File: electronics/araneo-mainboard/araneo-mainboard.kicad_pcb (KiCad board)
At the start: 2 copper layers, 71.5 x 68.5 mm, 77 parts, among them J1 GPIO2, J2 OLED, J3 GPIO1, SW2 SW, SW3 SW, U1 IMU, U3 TLV1117-ADJ, U4 POWER, U5 PAM8403D

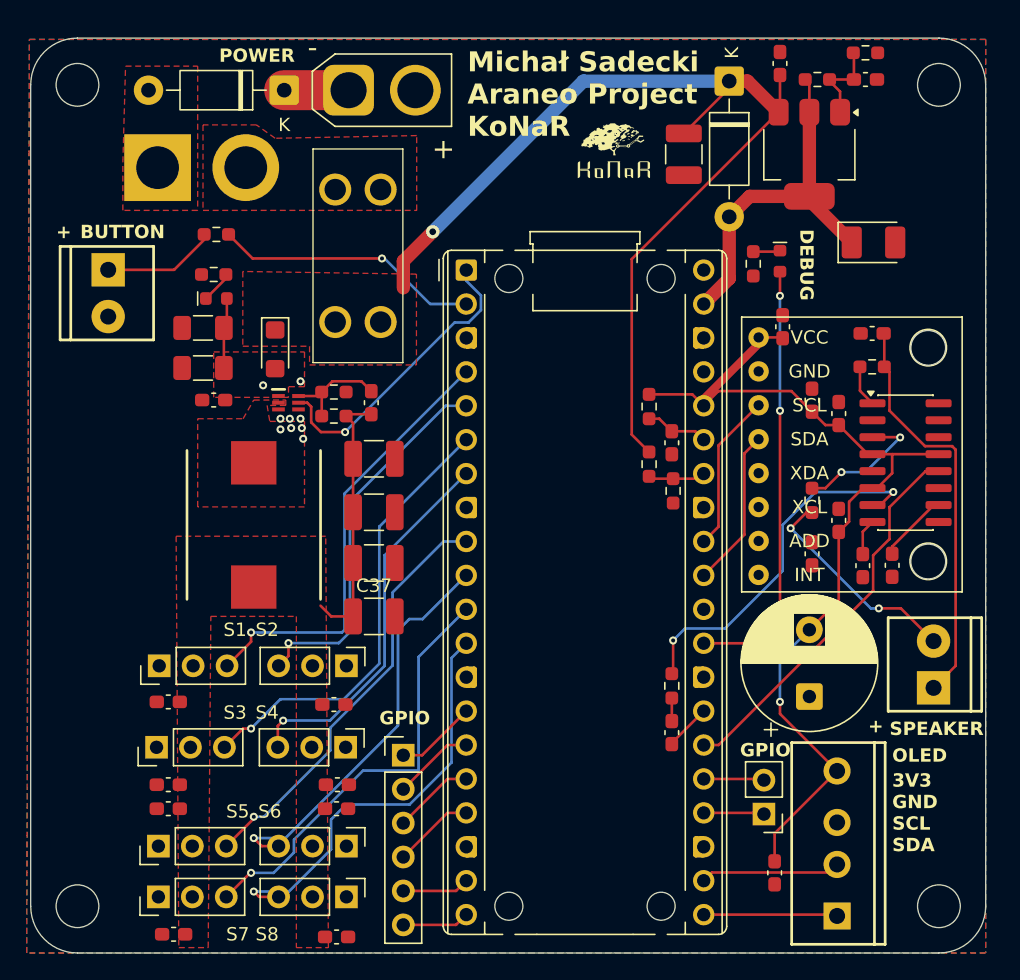
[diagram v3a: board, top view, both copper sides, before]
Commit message: electronics: add bmi270 and second buck
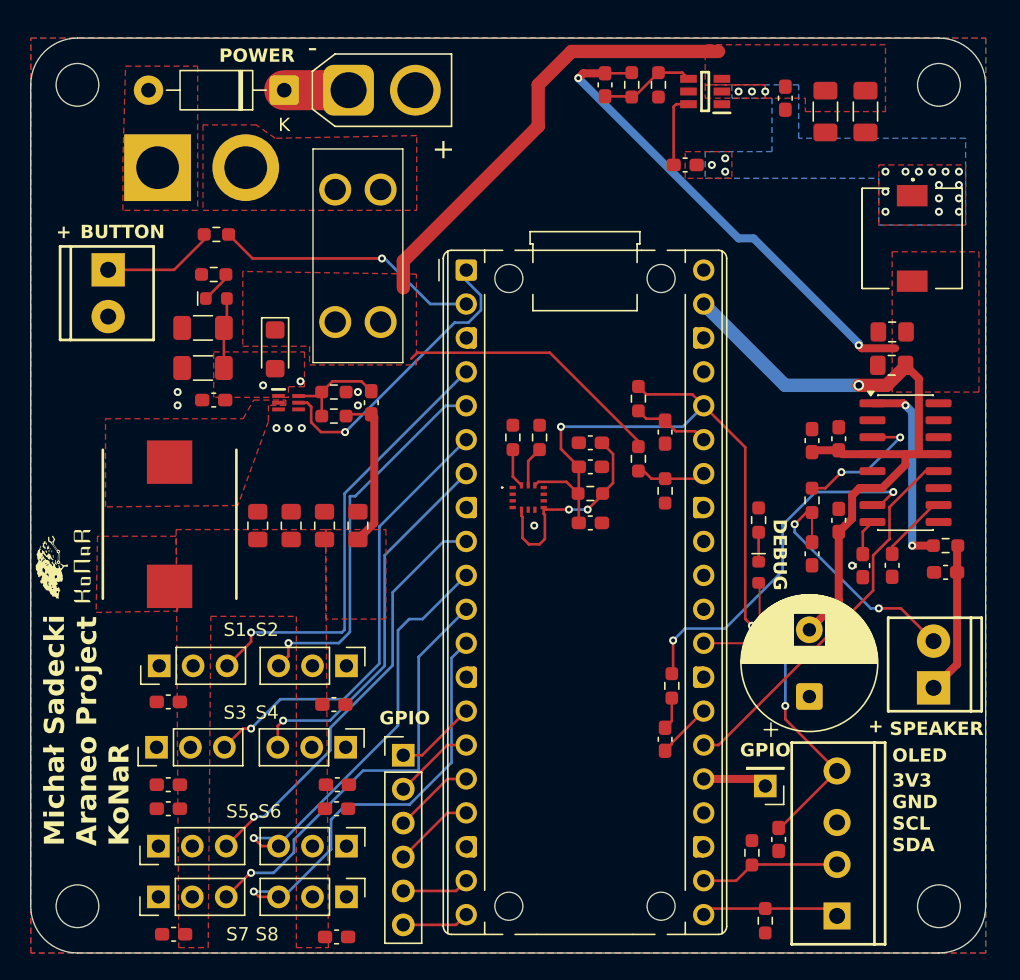
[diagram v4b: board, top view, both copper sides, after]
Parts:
- removed C2: 22uF, Capacitor_SMD:C_1210_3225Metric_Pad1.33x2.70mm_HandSolder
- removed D1: D, Diode_THT:D_DO-41_SOD81_P10.16mm_Horizontal
- removed R4: 120, Resistor_SMD:R_0603_1608Metric_Pad0.98x0.95mm_HandSolder
- removed R5: 360, Resistor_SMD:R_0603_1608Metric_Pad0.98x0.95mm_HandSolder
- removed U1: IMU, usini_sensors:module_mpu6050
- removed U3: TLV1117-ADJ, Package_TO_SOT_SMD:SOT-223-3_TabPin2
- added C35: 0.1u, Capacitor_SMD:C_0603_1608Metric_Pad1.08x0.95mm_HandSolder, F.Cu at (148.0, 40.0)
- added C39: 10u, Capacitor_SMD:C_1206_3216Metric_Pad1.33x1.80mm_HandSolder, F.Cu at (151.0, 41.0)
- added C40: 10u, Capacitor_SMD:C_1206_3216Metric_Pad1.33x1.80mm_HandSolder, F.Cu at (154.0, 41.0)
- added C41: 100p, Capacitor_SMD:C_0603_1608Metric_Pad1.08x0.95mm_HandSolder, F.Cu at (134.5, 39.0)
- added C42: 0.1u, Capacitor_SMD:C_0603_1608Metric_Pad1.08x0.95mm_HandSolder, F.Cu at (133.4, 67.6)
- added C43: 1u, Capacitor_SMD:C_0603_1608Metric_Pad1.08x0.95mm_HandSolder, F.Cu at (133.4, 71.8)
- added FB4: FerriteBead, Resistor_SMD:R_0603_1608Metric_Pad0.98x0.95mm_HandSolder, F.Cu at (133.4, 69.6)
- added IC1: TPS54302DDCR, custom_footprints:SOT95P280X110-6N, F.Cu at (142.0, 39.5)
- added IC2: BMI270, custom_footprints:BMI270, F.Cu at (128.8, 69.9)
- added L2: 10u, custom_footprints:PA4302103NLT, F.Cu at (157.5, 50.5)
- added R1: 4.7k, Resistor_SMD:R_0603_1608Metric_Pad0.98x0.95mm_HandSolder, F.Cu at (129.6, 65.4)
- added R16: 100k, Resistor_SMD:R_0603_1608Metric_Pad0.98x0.95mm_HandSolder, F.Cu at (136.5, 39.0)
- added R17: 13.3k, Resistor_SMD:R_0603_1608Metric_Pad0.98x0.95mm_HandSolder, F.Cu at (138.5, 39.0)
- added R18: 4.7k, Resistor_SMD:R_0603_1608Metric_Pad0.98x0.95mm_HandSolder, F.Cu at (146.5, 101.6)
- added R19: 4.7k, Resistor_SMD:R_0603_1608Metric_Pad0.98x0.95mm_HandSolder, F.Cu at (145.5, 96.5)
- added R2: 4.7k, Resistor_SMD:R_0603_1608Metric_Pad0.98x0.95mm_HandSolder, F.Cu at (127.6, 65.4)
- C1: value 22uF -> 0.1u; footprint Capacitor_Tantalum_SMD:CP_EIA-3528-15_AVX-H_HandSolder -> Capacitor_SMD:C_0603_1608Metric_Pad1.08x0.95mm_HandSolder
- C20: value 0.1uF -> 0.1u
- C29: value 1uF -> 22u; footprint Capacitor_SMD:C_0603_1608Metric_Pad1.08x0.95mm_HandSolder -> Capacitor_SMD:C_0805_2012Metric_Pad1.18x1.45mm_HandSolder
- C30: value 100nF -> 22u; footprint Capacitor_SMD:C_0603_1608Metric_Pad1.08x0.95mm_HandSolder -> Capacitor_SMD:C_0805_2012Metric_Pad1.18x1.45mm_HandSolder
- C34, C36, C37, C38: footprint Capacitor_SMD:C_1210_3225Metric_Pad1.33x2.70mm_HandSolder -> Capacitor_SMD:C_0805_2012Metric_Pad1.18x1.45mm_HandSolder
- C9: value 100nF -> 0.1u
- J3: footprint Connector_PinHeader_2.54mm:PinHeader_1x02_P2.54mm_Vertical -> Connector_PinHeader_2.54mm:PinHeader_1x01_P2.54mm_Vertical
- moved konar1 51.6 mm to (94.0, 75.0), turned to 90 degrees
- moved C1 26.0 mm to (133.4, 65.8)
- moved C30 24.1 mm to (156.0, 60.0), turned to 180 degrees
- moved D3 23.4 mm to (146.0, 75.5)
- moved R13 19.2 mm to (146.0, 71.6), turned to 90 degrees
- moved C29 19.0 mm to (156.0, 57.5), turned to 180 degrees
- moved C11 18.7 mm to (160.0, 75.5)
- moved FB1 14.5 mm to (160.0, 73.5)
- moved C20 14.1 mm to (140.5, 45.0), turned to 180 degrees
- moved C37 11.0 mm to (108.5, 72.0), turned to 90 degrees
- moved C36 6.80 mm to (111.0, 72.0), turned to 90 degrees
- moved L1 6.30 mm to (101.9, 71.9)
- moved C34 5.14 mm to (116.0, 72.0), turned to 90 degrees
- moved C38 3.83 mm to (113.5, 72.0), turned to 90 degrees
- moved C18 3.03 mm to (150.0, 65.6)
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- gave numbers to parts that had none: 1
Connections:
- A1 pad 24: /GPIO18 -> /IMU_INT1
- A1 pad 31: /SDA_IMU -> /IMU_SDA
- A1 pad 32: /SCL_IMU -> /IMU_SCL
- C1 pad 1: +5V -> GND
- C1 pad 2: GND -> Net-(IC2-VDD)
- C15 pad 1: +3V3 -> +5V
- C16 pad 2: +3V3 -> +5V
- C17 pad 2: +3V3 -> +5V
- C18 pad 2: +3V3 -> +5V
- C20 pad 1: +3V3 -> Net-(IC1-SW)
- C20 pad 2: GND -> Net-(IC1-BOOT)
- C29 pad 1: Net-(U3-ADJ) -> +5V
- C30 pad 1: +7.4V_F -> +5V
- J3 pad 1: /GPIO18 -> /GPIO19
- U5 pad 13: +3V3 -> +5V
- U5 pad 4: +3V3 -> +5V
- U5 pad 6: +3V3 -> +5V
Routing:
- net +5V: track 27.6 -> 88.5 mm, vias 0 -> 3
- net /D1: track 32.9 -> 8.11 mm, vias 2 -> 0
- net +7.4V_F: track 75.3 -> 54.3 mm, vias 1 -> 0
- net Net-(C11-Pad2): track 30.6 -> 11.4 mm
- net Net-(IC2-VDD): track 0.00 -> 16.1 mm, vias 0 -> 2
- net /SDA_IMU: track 11.9 -> 0.00 mm
- net /SCL_IMU: track 11.9 -> 0.00 mm
- net Net-(U5-LOUT+): track 3.12 -> 14.8 mm, vias 0 -> 2
- net +6V: track 19.9 -> 11.9 mm
- net Net-(IC1-FB): track 0.00 -> 7.22 mm
- net Net-(U3-ADJ): track 6.62 -> 0.00 mm
- net +3V3: track 71.5 -> 66.0 mm, vias 1 -> 3
- net Net-(IC1-BOOT): track 0.00 -> 5.55 mm
- net /GPIO18: track 4.55 -> 0.00 mm
- net /IMU/IMU_SCL: track 0.00 -> 3.03 mm
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- added copper zone on F.Cu, net +5V
- added copper zone on B.Cu, net Net-(IC1-SW)
- added copper zone on F.Cu, net Net-(IC1-SW)
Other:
- board text added: "15.07.2026-04.08.2026 Projekt inżynierski prowadzony przez Mateusza Cholewińskiego"
- board text removed: "22.07.2026 Projekt inżynierski prowadzony przez Mateusza Cholewińskiego"

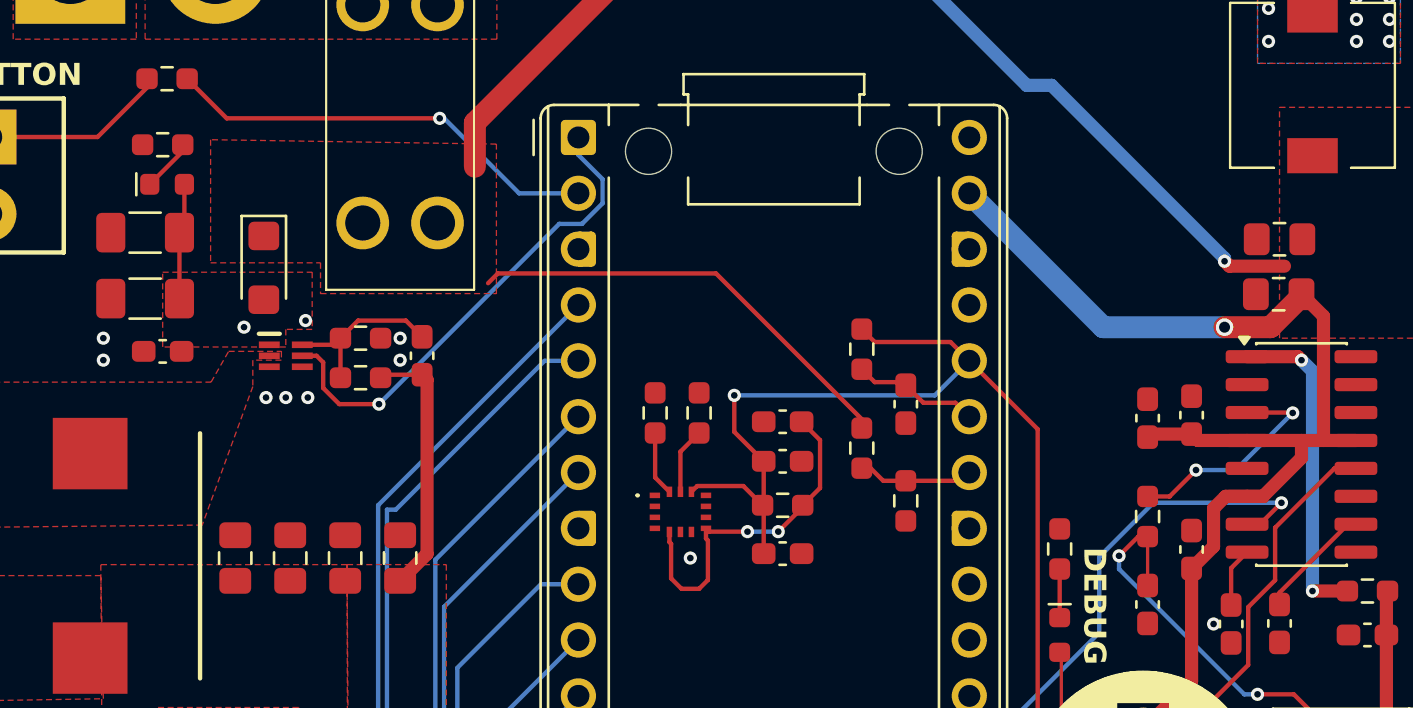
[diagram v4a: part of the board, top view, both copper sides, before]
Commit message: electronics: add diode indicator
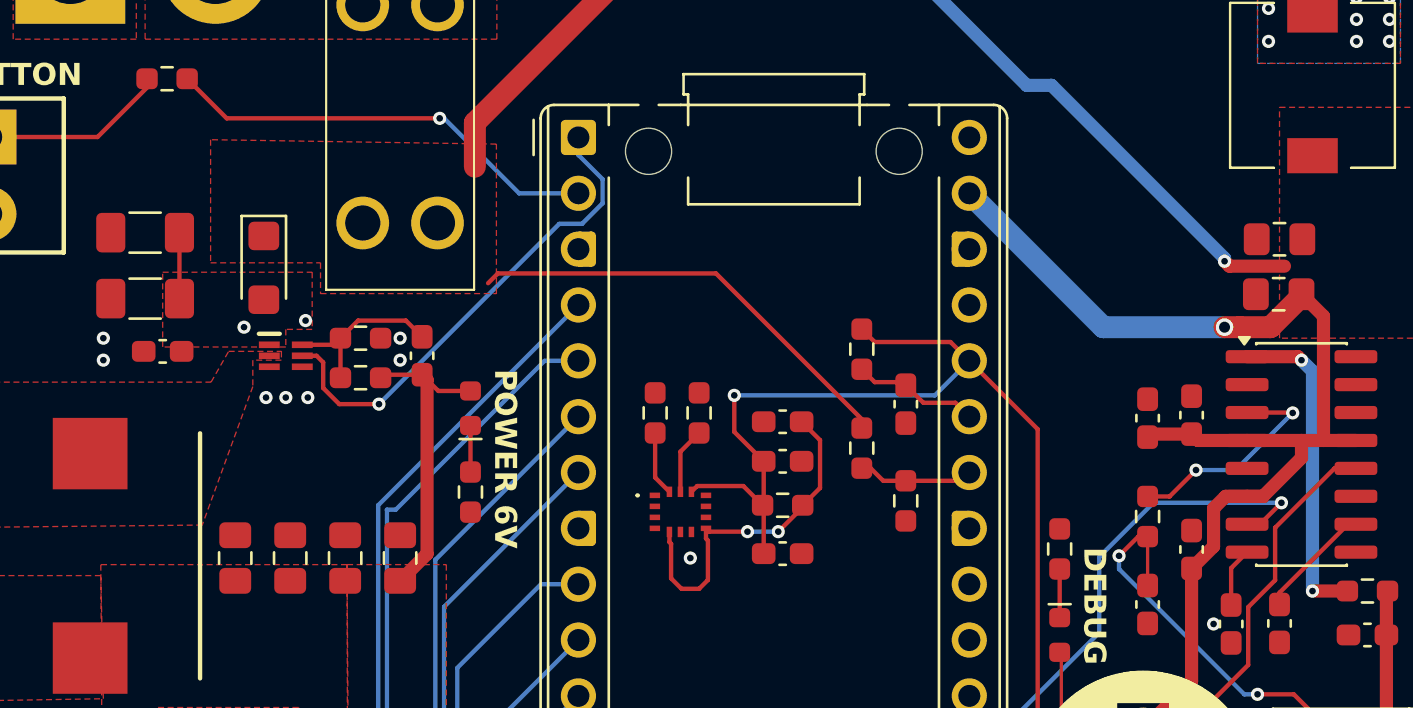
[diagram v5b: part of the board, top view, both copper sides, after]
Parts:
- moved R15 21.1 mm to (119.2, 69.0), turned to 90 degrees
- moved D5 17.2 mm to (119.2, 65.2), turned to 90 degrees
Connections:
- D5 pad 2: Net-(D2-A2) -> +6V
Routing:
- net +6V: track 11.9 -> 14.4 mm
- net Net-(D2-A2): track 5.80 -> 3.82 mm
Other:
- board text added: "POWER 6V"
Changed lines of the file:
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@@
 	(footprint "PCM_SparkFun-LED:LED_0603_1608Metric"
 		(layer "F.Cu")
-		(at 105.4 55)
+		(at 119.2 65.1875 90)
 		(tags "SparkFun LED")
 		(property "Reference" "D5"
-			(at 0 -1.43 0)
+			(at 0 -1.43 90)
 			(layer "F.Fab")
 			(effects
@@
 		)
 		(property "Value" "POWER_LED"
-			(at 0 1.43 0)
+			(at 0 1.43 90)
 			(layer "F.Fab")
 			(effects
@@
 		)
 		(property "Datasheet" ""
-			(at 0 0 0)
+			(at 0 0 90)
 			(unlocked yes)
 			(layer "F.Fab")
@@
 		)
 		(property "Description" "Light emitting diode"
-			(at 0 0 0)
+			(at 0 0 90)
 			(unlocked yes)
 			(layer "F.Fab")
@@
 		)
 		(property "PROD_ID" "LED-"
-			(at 0 0 0)
+			(at 0 0 90)
 			(unlocked yes)
 			(layer "F.Fab")
@@
 		)
 		(fp_line
-			(start -1.48 -0.73)
-			(end 1.48 -0.73)
+			(start 1.48 -0.73)
+			(end 1.48 0.73)
 			(stroke
 				(width 0.05)
@@
 		)
 		(fp_line
-			(start -1.48 0.73)
-			(end -1.48 -0.73)
+			(start -1.48 -0.73)
+			(end 1.48 -0.73)
 			(stroke
 				(width 0.05)
@@
 		)
 		(fp_line
-			(start 1.48 -0.73)
-			(end 1.48 0.73)
+			(start 1.48 0.73)
+			(end -1.48 0.73)
 			(stroke
 				(width 0.05)
@@
 		)
 		(fp_line
-			(start 1.48 0.73)
-			(end -1.48 0.73)
+			(start -1.48 0.73)
+			(end -1.48 -0.73)
 			(stroke
 				(width 0.05)
@@
 		)
 		(fp_line
-			(start -0.8 -0.1)
-			(end -0.8 0.4)
+			(start 0.8 -0.4)
+			(end -0.5 -0.4)
 			(stroke
 				(width 0.1)
@@
 		)
 		(fp_line
-			(start -0.8 0.4)
-			(end 0.8 0.4)
+			(start -0.5 -0.4)
+			(end -0.8 -0.1)
 			(stroke
 				(width 0.1)
@@
 		)
 		(fp_line
-			(start -0.5 -0.4)
-			(end -0.8 -0.1)
+			(start -0.8 -0.1)
+			(end -0.8 0.4)
 			(stroke
 				(width 0.1)
@@
 		)
 		(fp_line
-			(start 0.8 -0.4)
-			(end -0.5 -0.4)
+			(start 0.8 0.4)
+			(end 0.8 -0.4)
 			(stroke
 				(width 0.1)
@@
 		)
 		(fp_line
-			(start 0.8 0.4)
-			(end 0.8 -0.4)
+			(start -0.8 0.4)
+			(end 0.8 0.4)
 			(stroke
 				(width 0.1)
@@
 		)
 		(pad "1" smd roundrect
-			(at -0.7875 0)
+			(at -0.7875 0 90)
 			(size 0.875 0.95)
 			(layers "F.Cu" "F.Mask" "F.Paste")
@@
 		)
 		(pad "2" smd roundrect
-			(at 0.7875 0)
+			(at 0.7875 0 90)
 			(size 0.875 0.95)
 			(layers "F.Cu" "F.Mask" "F.Paste")
 			(roundrect_rratio 0.25)
-			(net "Net-(D2-A2)")
+			(net "+6V")
 			(pinfunction "A_2")
 			(pintype "passive")
@@
 	(footprint "Resistor_SMD:R_0603_1608Metric_Pad0.98x0.95mm_HandSolder"
 		(layer "F.Cu")
-		(at 105.2 53.2)
+		(at 119.2 69 90)
 		(descr "Resistor SMD 0603 (1608 Metric), square (rectangular) end terminal, IPC-7351 nominal with elongated pad for handsoldering. (Body size source: IPC-SM-782 page 72, https://www.pcb-3d.com/wordpress/wp-content/uploads/ipc-sm-782a_amendment_1_and_2.pdf)")
 		(tags "resistor handsolder")
 		(property "Reference" "R15"
-			(at 0 -1.43 0)
+			(at 0 -1.43 90)
 			(layer "F.SilkS")
 			(hide yes)
@@
 		)
 		(property "Value" "1k"
-			(at 0 1.43 0)
+			(at 0 1.43 90)
 			(layer "F.Fab")
 			(effects
@@
 		)
 		(property "Datasheet" ""
-			(at 0 0 0)
+			(at 0 0 90)
 			(layer "F.Fab")
 			(hide yes)
@@
 		)
 		(property "Description" "Resistor"
-			(at 0 0 0)
+			(at 0 0 90)
 			(layer "F.Fab")
 			(hide yes)
@@
 		)
 		(fp_text user "${REFERENCE}"
-			(at 0 0 0)
+			(at 0 0 90)
 			(layer "F.Fab")
 			(effects
@@
 		)
 		(pad "1" smd roundrect
-			(at -0.9125 0)
+			(at -0.9125 0 90)
 			(size 0.975 0.95)
 			(layers "F.Cu" "F.Mask" "F.Paste")
@@
 		)
 		(pad "2" smd roundrect
-			(at 0.9125 0)
+			(at 0.9125 0 90)
 			(size 0.975 0.95)
 			(layers "F.Cu" "F.Mask" "F.Paste")
@@
 		)
 	)
+	(gr_text "POWER 6V"
+		(at 120.2 63.4 270)
+		(layer "F.SilkS" knockout)
+		(effects
+			(font
+				(size 1 1)
+				(thickness 0.2)
+				(bold yes)
+			)
+			(justify left bottom)
+		)
+	)
 	(gr_text "BUTTON"
 		(at 95.2 50.6 0)
@@
 	)
 	(segment
+		(start 117.7375 64.4)
+		(end 117 63.6625)
+		(width 0.2)
+		(layer "F.Cu")
+		(net "+6V")
+	)
+	(segment
 		(start 117.225 71.8125)
 		(end 117.225 63.8875)
@@
 	)
 	(segment
-		(start 106.1125 53.2)
-		(end 106.1125 53.5)
+		(start 119.2 64.4)
+		(end 117.7375 64.4)
 		(width 0.2)
 		(layer "F.Cu")
-		(net "Net-(D5-K)")
+		(net "+6V")
 	)
 	(segment
-		(start 106.1125 53.5)
-		(end 104.6125 55)
+		(start 119.2 65.975)
+		(end 119.2 68.0875)
 		(width 0.2)
 		(layer "F.Cu")
@@
 	)
 	(segment
-		(start 106.1875 55)
-		(end 106.1875 56.975)
-		(width 0.2)
-		(layer "F.Cu")
-		(net "Net-(D2-A2)")
-	)
-	(segment
 		(start 105.9625 60.5625)
 		(end 106.0625 60.6625)
@@
 	(segment
 		(start 155.58793 61.5)
+		(end 154.2 61.5)
+		(width 1)
+		(layer "F.Cu")
+		(net "+5V")
+	)
+	(segment
+		(start 154.2 61.5)
 		(end 153.5 61.5)
 		(width 1)
@@
 	)
 	(segment
+		(start 127.6 68.337)
+		(end 128.25 68.987)
+		(width 0.2)
+		(layer "F.Cu")
+		(net "/IMU/IMU_SDA")
+	)
+	(segment
+		(start 127.6 66.3125)
+		(end 127.6 68.337)
+		(width 0.2)
+		(layer "F.Cu")
+		(net "/IMU/IMU_SDA")
+	)
+	(segment
 		(start 106.2 82.5)
 		(end 108 80.7)
@@
 		(net "/GPIO19")
 	)
-	(segment
-		(start 127.6 68.337)
-		(end 128.25 68.987)
-		(width 0.2)
-		(layer "F.Cu")
-		(net "/IMU/IMU_SDA")
-	)
-	(segment
-		(start 127.6 66.3125)
-		(end 127.6 68.337)
-		(width 0.2)
-		(layer "F.Cu")
-		(net "/IMU/IMU_SDA")
-	)
 	(zone
